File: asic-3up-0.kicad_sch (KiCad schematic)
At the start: 78 parts, among them J12 Conn_01x01, J13 Conn_01x01, J18 Conn_01x01, J19 Conn_01x01, J3 Conn_01x01, J4 Conn_01x01, U28 MCP1824T-1202E/OT, U29 MCP1824T-1202E/OT, U30 MCP1824T-1202E/OT, U32 MCP1824T-0802E, U42 MCP1824T-0802E, U43 MCP1824T-0802E, U45 BM1362AC_MODE1, U46 BM1362AC_MODE0, U47 BM1362AC_MODE1

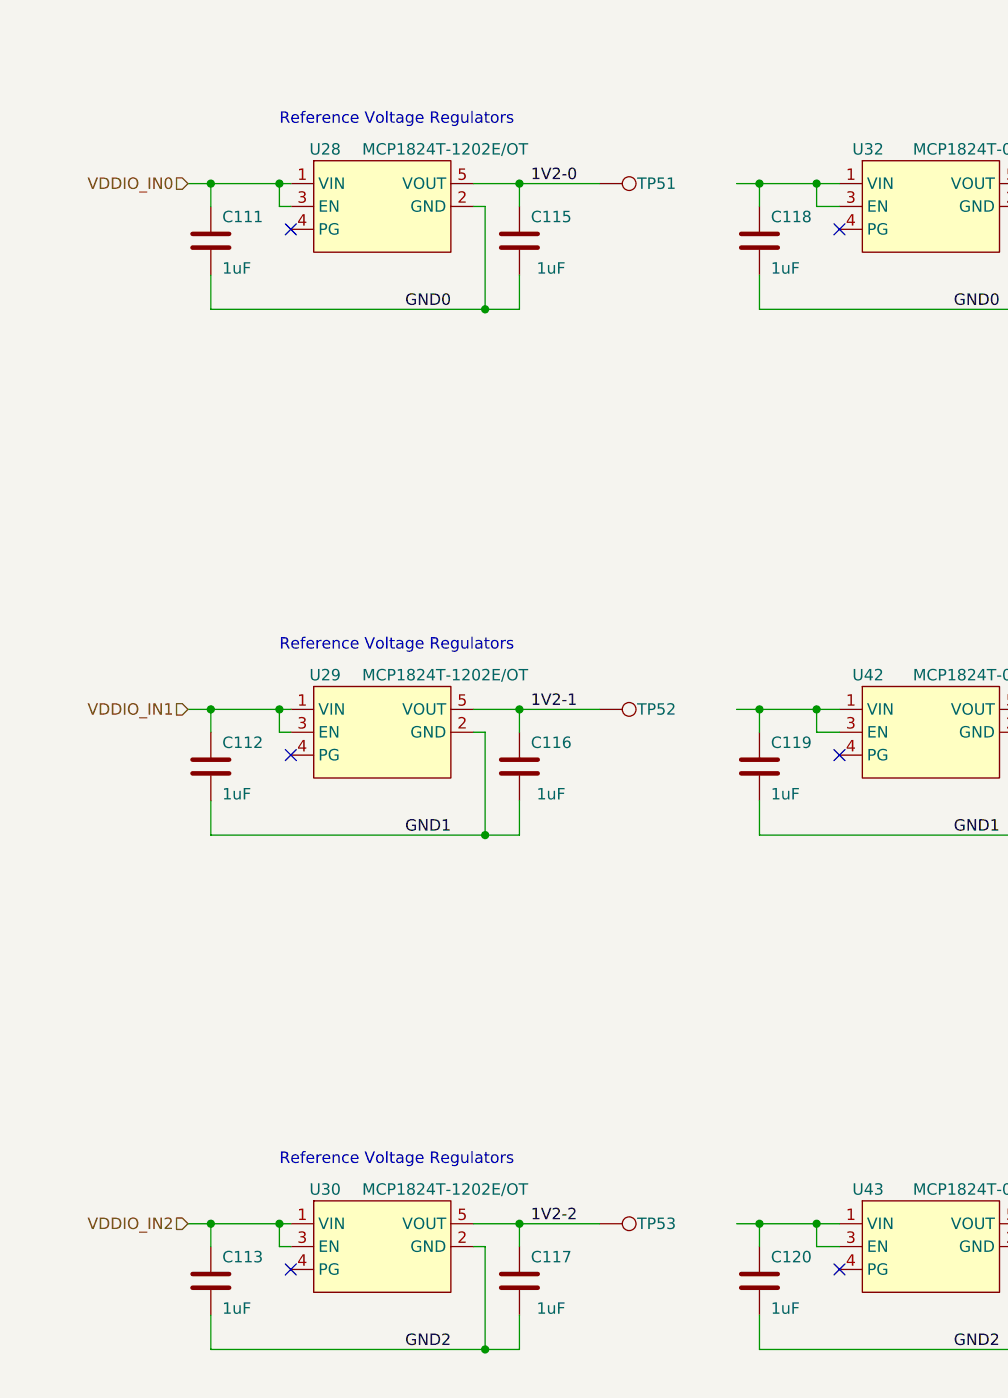
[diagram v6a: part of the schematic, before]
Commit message: added temp sensors. wired up (hopeful) vreg EN circuit. lots of LDO routing.
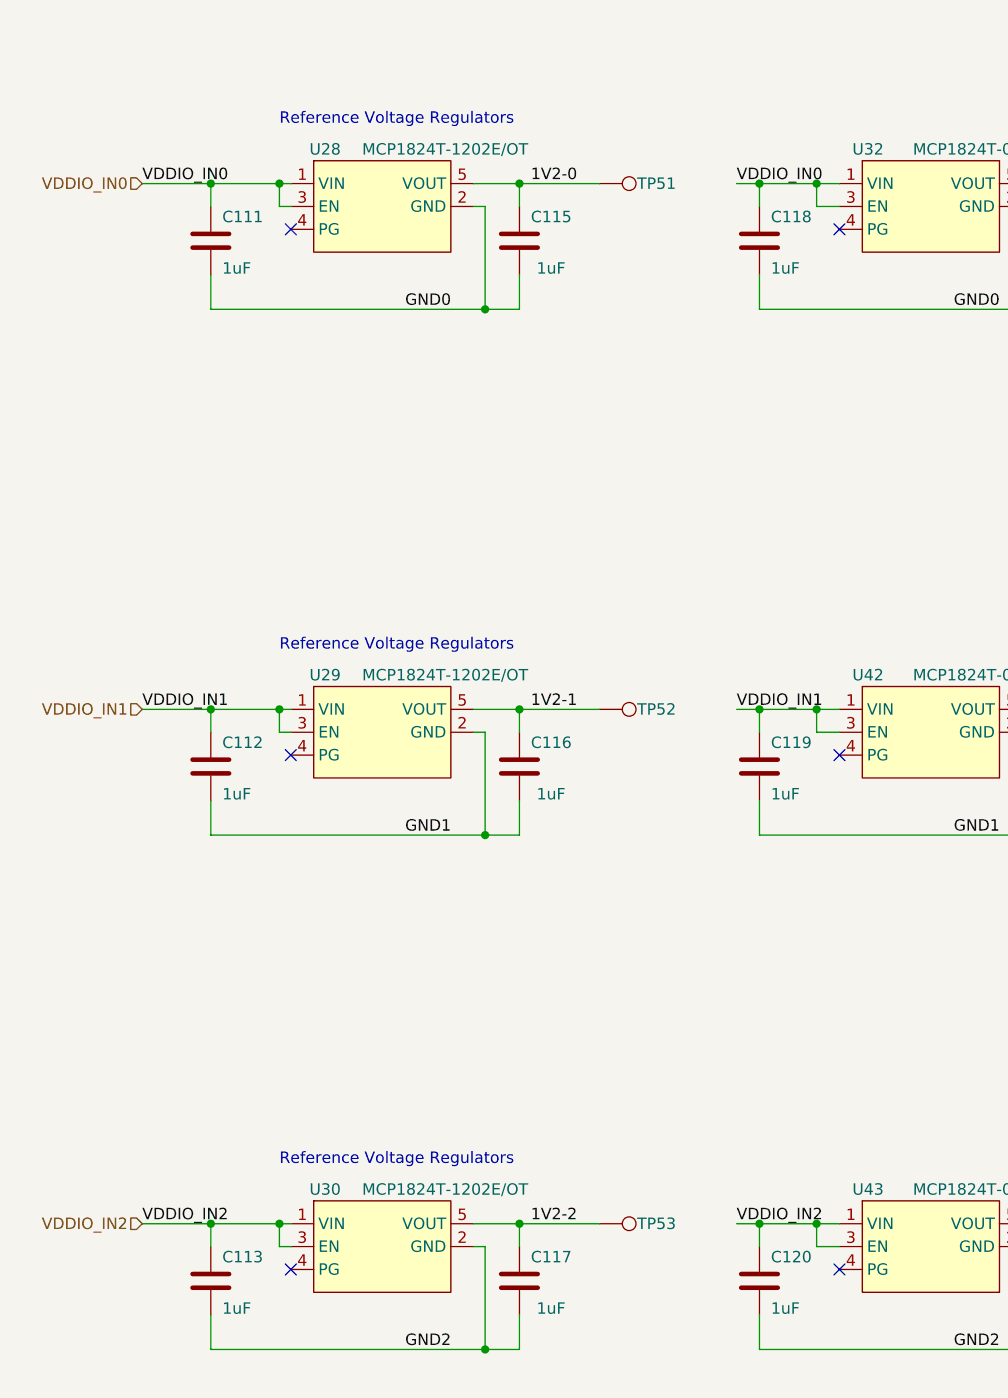
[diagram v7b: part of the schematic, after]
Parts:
- J18: footprint emberone:5x9_powertab -> emberone:14x9_powertab_L
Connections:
- net VDDIO_IN0: now also C118.1, U32.1 (VIN), U32.3 (EN)
- net VDDIO_IN1: now also C119.1, U42.1 (VIN), U42.3 (EN)
- net VDDIO_IN2: now also C120.1, U43.1 (VIN), U43.3 (EN)
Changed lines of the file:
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@@
 	(wire
 		(pts
-			(xy 31.75 168.91) (xy 34.29 168.91)
+			(xy 26.67 168.91) (xy 34.29 168.91)
 		)
 		(stroke
@@
 	(wire
 		(pts
-			(xy 31.75 110.49) (xy 34.29 110.49)
+			(xy 26.67 110.49) (xy 34.29 110.49)
 		)
 		(stroke
@@
 	(wire
 		(pts
-			(xy 31.75 226.06) (xy 34.29 226.06)
+			(xy 26.67 226.06) (xy 34.29 226.06)
 		)
 		(stroke
@@
 		)
 	)
+	(label "VDDIO_IN2"
+		(at 26.67 226.06 0)
+		(fields_autoplaced yes)
+		(effects
+			(font
+				(size 1.27 1.27)
+			)
+			(justify left bottom)
+		)
+	)
 	(label "1V2-2"
 		(at 69.85 226.06 0)
@@
 		)
 	)
+	(label "VDDIO_IN0"
+		(at 92.71 110.49 0)
+		(fields_autoplaced yes)
+		(effects
+			(font
+				(size 1.27 1.27)
+			)
+			(justify left bottom)
+		)
+	)
 	(label "GND0"
 		(at 196.85 102.87 0)
@@
 		)
 	)
+	(label "VDDIO_IN2"
+		(at 92.71 226.06 0)
+		(fields_autoplaced yes)
+		(effects
+			(font
+				(size 1.27 1.27)
+			)
+			(justify left bottom)
+		)
+	)
+	(label "VDDIO_IN1"
+		(at 92.71 168.91 0)
+		(fields_autoplaced yes)
+		(effects
+			(font
+				(size 1.27 1.27)
+			)
+			(justify left bottom)
+		)
+	)
 	(label "0V8-0"
 		(at 132.08 110.49 0)
@@
 		)
 	)
+	(label "VDDIO_IN0"
+		(at 26.67 110.49 0)
+		(fields_autoplaced yes)
+		(effects
+			(font
+				(size 1.27 1.27)
+			)
+			(justify left bottom)
+		)
+	)
 	(label "3V6"
 		(at 222.25 92.71 180)
@@
 		)
 	)
+	(label "VDDIO_IN1"
+		(at 26.67 168.91 0)
+		(fields_autoplaced yes)
+		(effects
+			(font
+				(size 1.27 1.27)
+			)
+			(justify left bottom)
+		)
+	)
 	(label "1V2-0"
 		(at 199.39 130.81 0)
@@
 	(hierarchical_label "VDDIO_IN0"
 		(shape input)
-		(at 31.75 110.49 180)
+		(at 26.67 110.49 180)
 		(fields_autoplaced yes)
 		(effects
@@
 	(hierarchical_label "VDDIO_IN1"
 		(shape input)
-		(at 31.75 168.91 180)
+		(at 26.67 168.91 180)
 		(fields_autoplaced yes)
 		(effects
@@
 	(hierarchical_label "VDDIO_IN2"
 		(shape input)
-		(at 31.75 226.06 180)
+		(at 26.67 226.06 180)
 		(fields_autoplaced yes)
 		(effects
@@
 			)
 		)
-		(property "Footprint" "emberone:5x9_powertab"
+		(property "Footprint" "emberone:14x9_powertab_L"
 			(at 231.14 92.71 0)
 			(effects

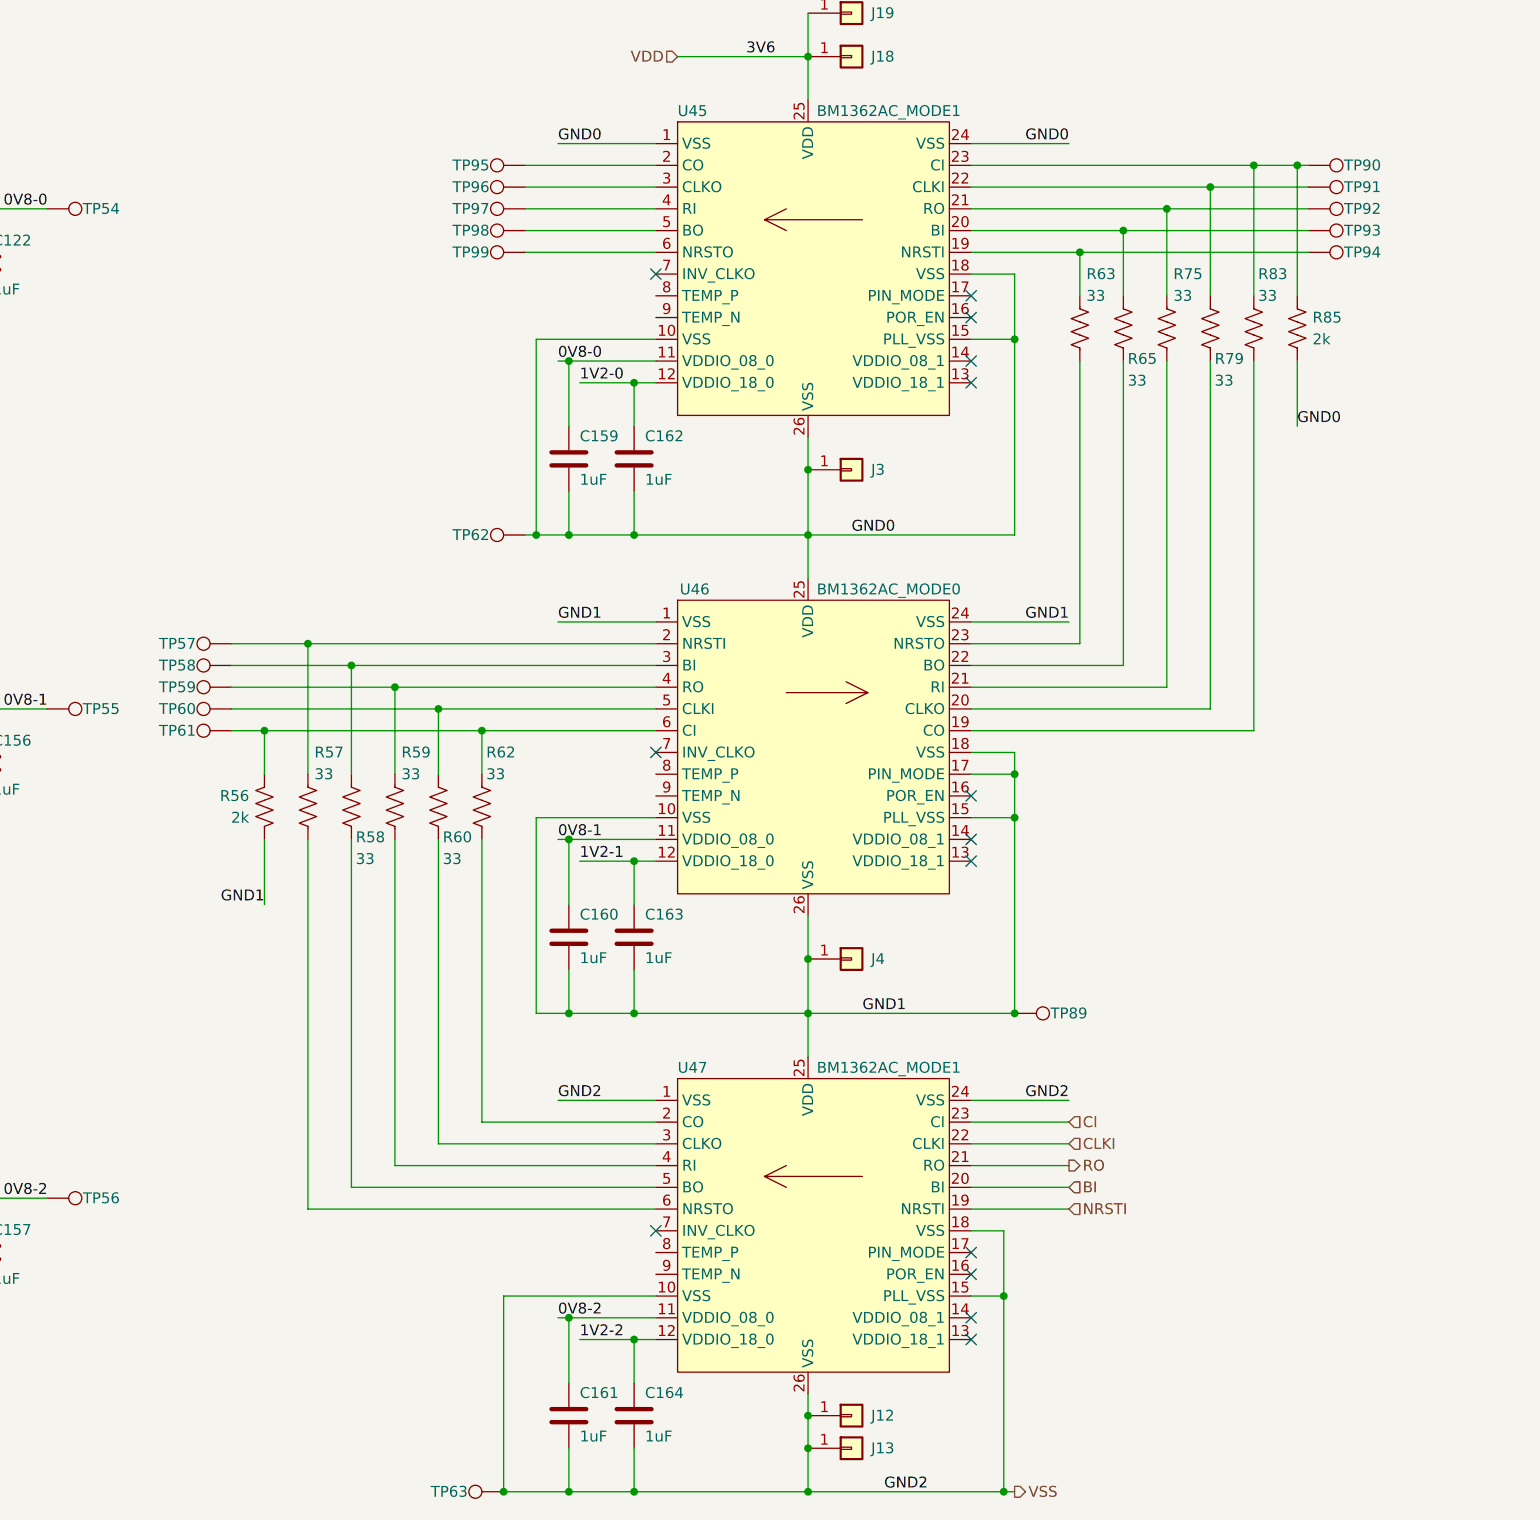
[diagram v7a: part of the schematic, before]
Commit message: all placed *almost* all routed
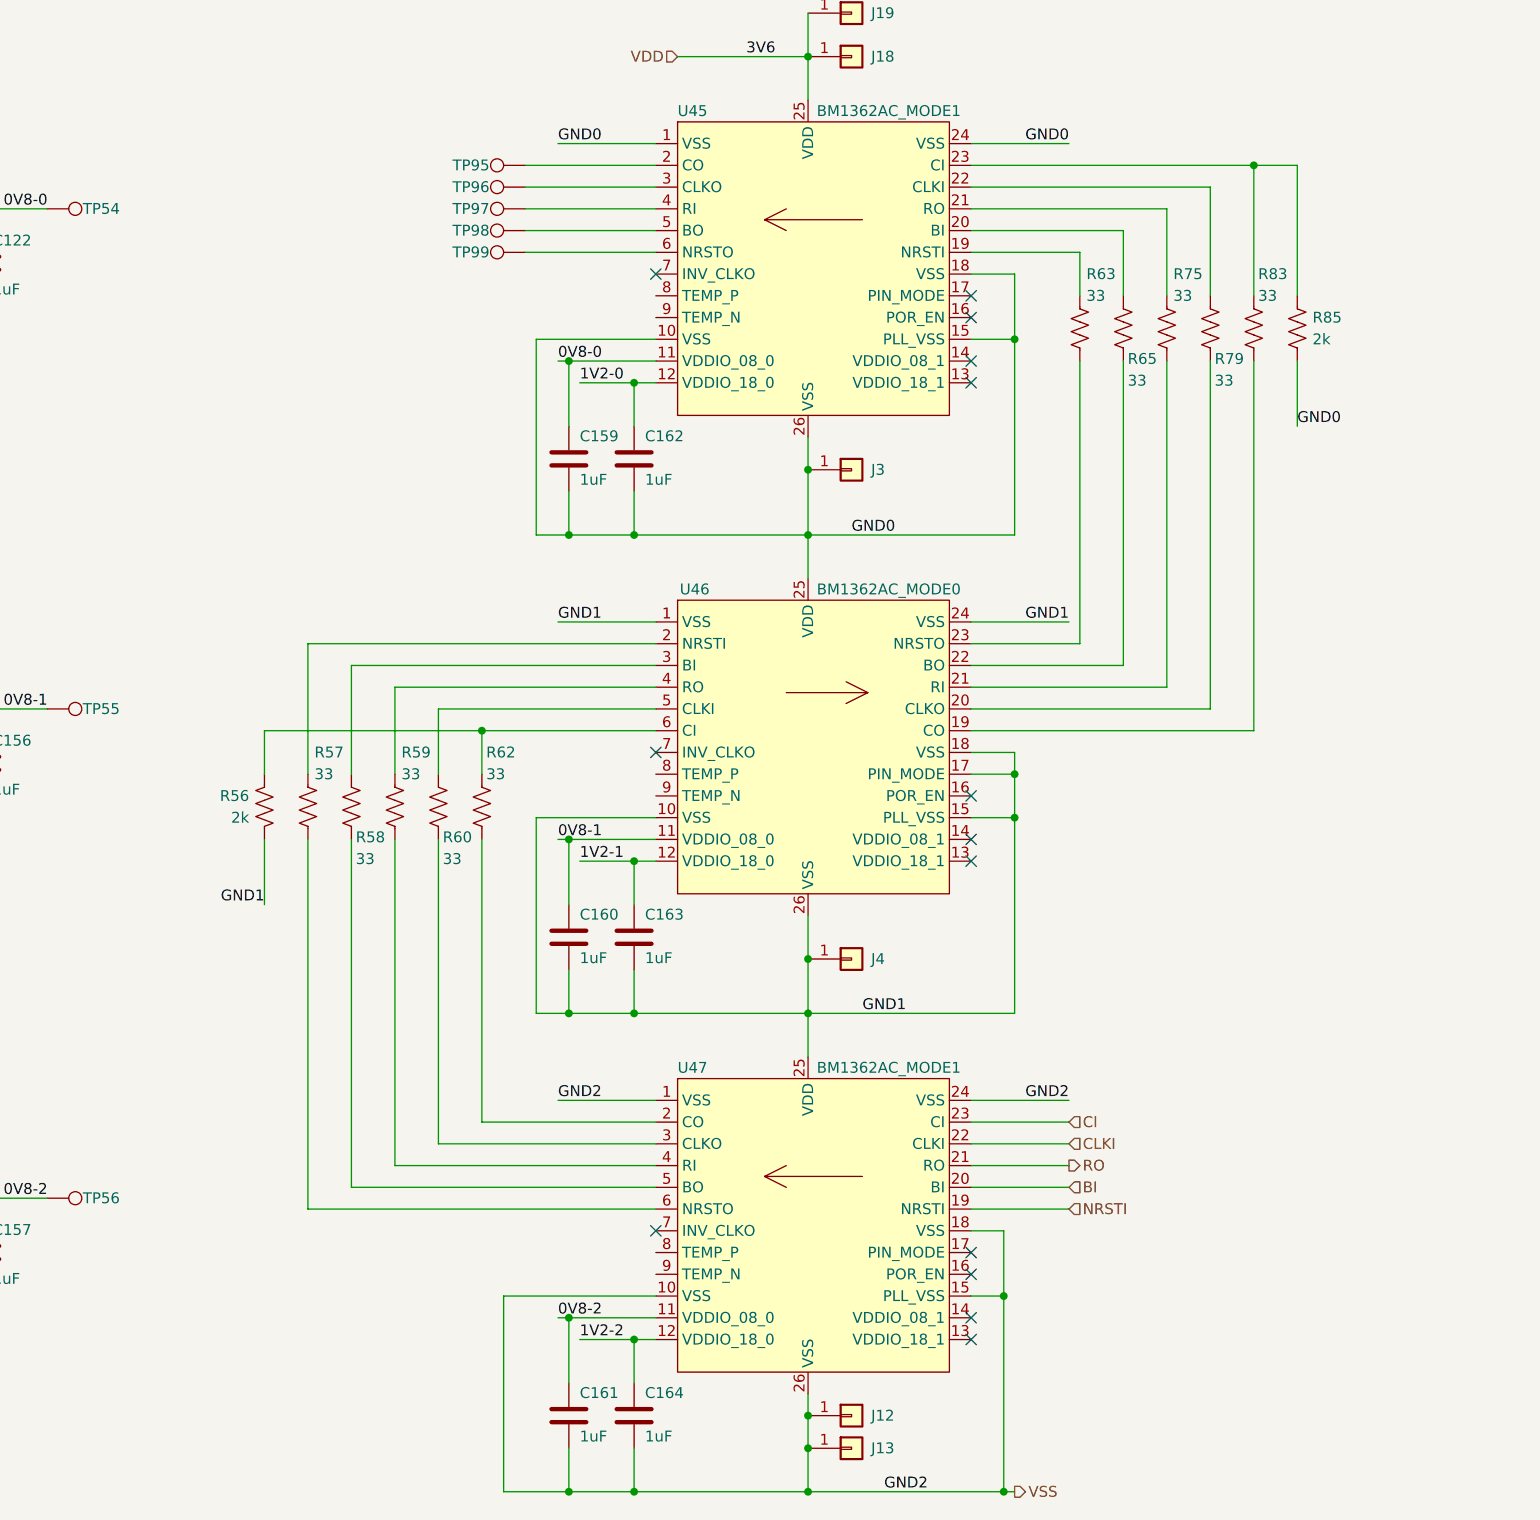
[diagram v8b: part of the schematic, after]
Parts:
- removed TP57, TP58, TP59, TP60, TP61, TP62, TP63, TP89, TP90, TP91, TP92, TP93, TP94: TestPoint, TestPoint:TestPoint_Pad_D1.0mm, symbol Connector:TestPoint
